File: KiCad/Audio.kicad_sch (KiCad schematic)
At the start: 56 parts, among them J10 Game/MIDI, J17 CD In, J18 Wave Table, J7 Line In, J8 Mic In, J9 Line Out, U19 AD1816AJS, Y4 24MHz

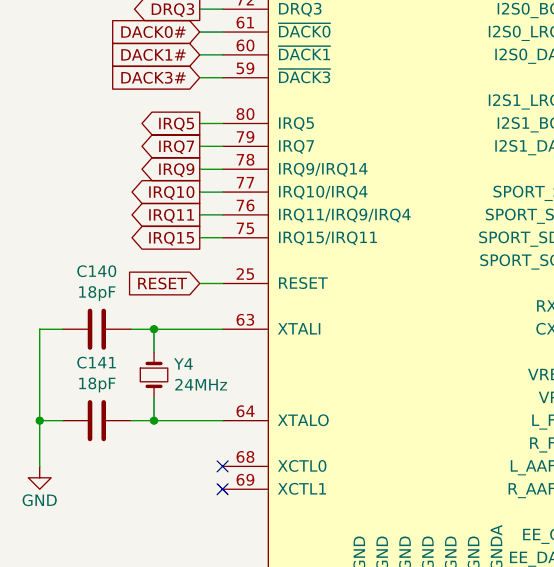
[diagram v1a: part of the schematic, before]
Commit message: Version 0.4: Update chipset connection
Signed-off-by: Sergey Kiselev <skiselev@gmail.com>
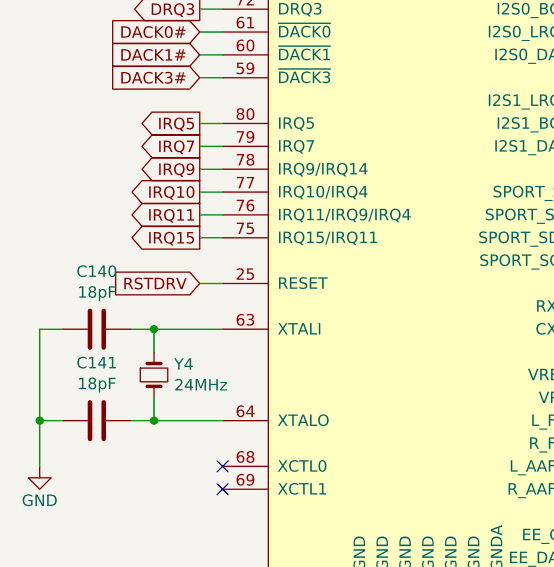
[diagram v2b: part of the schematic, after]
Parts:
- C140, C141, C143, C145, C146, C147, C148, C149, C150, C153, C154, C155, C156, C157, C158, C159, C160, C161, C162, C163, C164, C165, C166, C167, C169, C170: footprint (none) -> Capacitor_SMD:C_0603_1608Metric_Pad1.08x0.95mm_HandSolder
- C142, C144, C168: footprint (none) -> Capacitor_THT:CP_Radial_D5.0mm_P2.00mm; symbol Device:CP1 -> Device:C_Polarized_US
- C151, C152: footprint (none) -> Capacitor_THT:CP_Radial_D5.0mm_P2.00mm
- J10: footprint (none) -> Connector_Dsub:DSUB-15_Female_Horizontal_P2.77x2.84mm_EdgePinOffset4.94mm_Housed_MountingHolesOffset7.48mm
- J17: footprint (none) -> My_Components:Conn_Pin_Header_4x1_2.54mm
- J18: footprint (none) -> My_Components:Conn_Pin_Header_13x2_2.54mm
- J7, J8, J9: footprint (none) -> My_Components:Conn_Audio_3.5mm_Stereo_SJ1-352XNG
- JP18: footprint (none) -> My_Components:Conn_Pin_Header_2x1_2.54mm
- R141, R142, R143, R144, R145, R146, R147, R148, R149, R150, R151, R152, R153, R154, R155, R156: footprint (none) -> Resistor_SMD:R_0612_1632Metric_Pad1.18x3.40mm_HandSolder
- U19: footprint (none) -> My_Components:IC_PQFP-100_14x20mm_P0.65mm_Hand_Soldering
- Y4: footprint (none) -> My_Components:Crystal_HC-49U_Vert
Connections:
- net RESET renamed RSTDRV

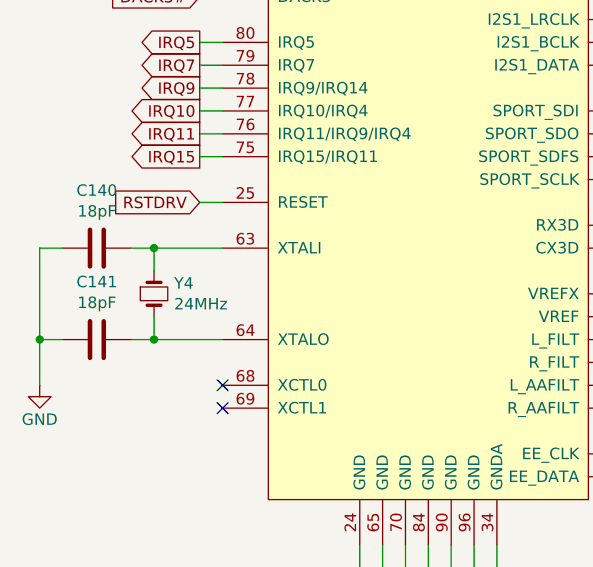
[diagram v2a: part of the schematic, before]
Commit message: More schematic updates. Remove old KiCad files
Signed-off-by: Sergey Kiselev <skiselev@gmail.com>
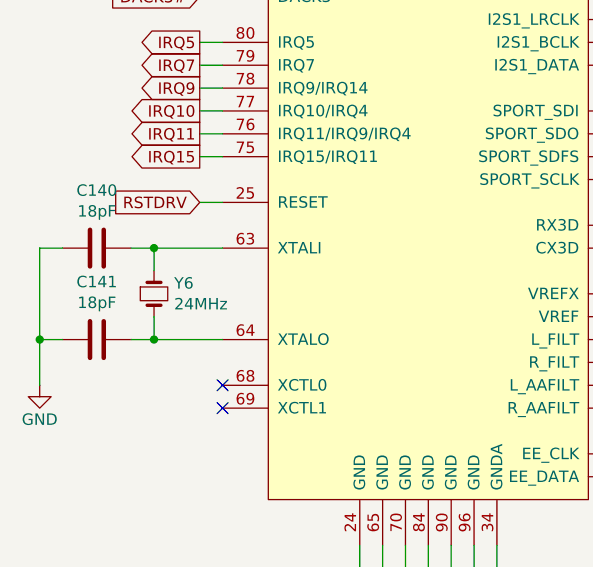
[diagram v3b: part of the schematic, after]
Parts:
- renumbered Y4 to Y6
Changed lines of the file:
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@@
   (symbol (lib_id "Device:Crystal_Small") (at 27.94 154.94 270) (unit 1)
     (in_bom yes) (on_board yes)
-    (property "Reference" "Y4" (id 0) (at 30.1752 153.7716 90)
+    (property "Reference" "Y6" (id 0) (at 30.1752 153.7716 90)
       (effects (font (size 1.27 1.27)) (justify left))
     )
